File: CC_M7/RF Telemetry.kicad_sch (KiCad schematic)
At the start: 33 parts, among them J9 SMA_CONNECTOR, U6 nRF52820-QDxx, U7 NRF21540-QDAA-R7, Y2 32MHz

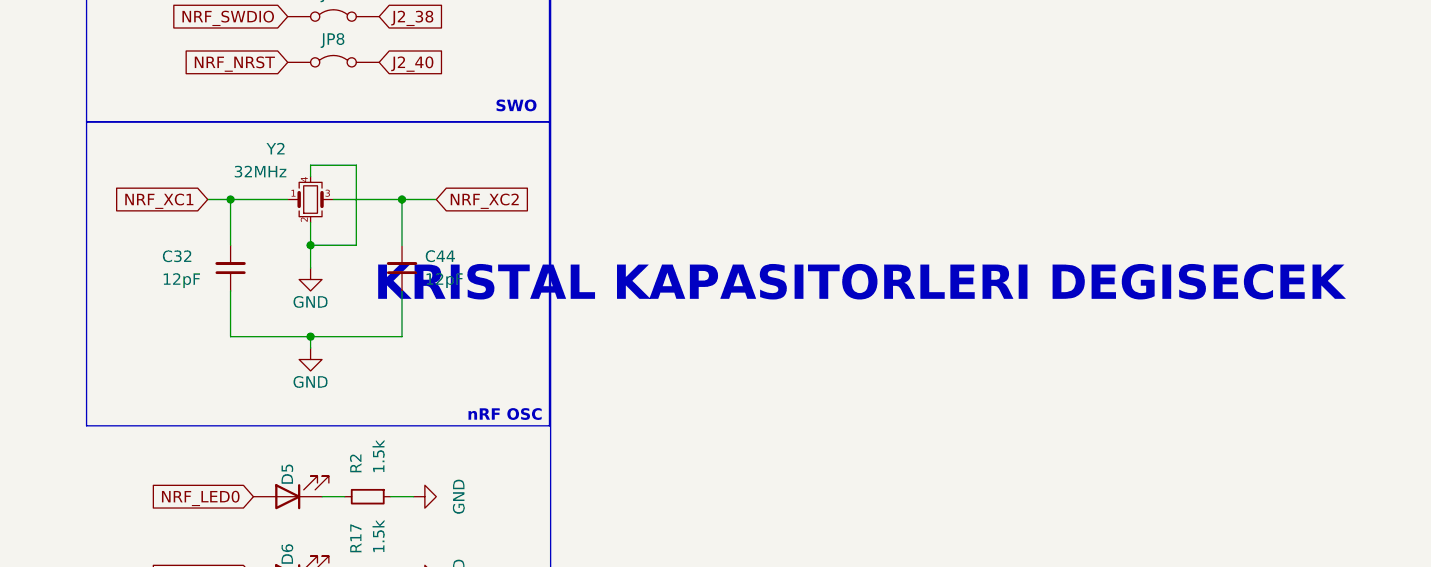
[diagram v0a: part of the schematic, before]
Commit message: USB Pullup added, oscillator capacitors updated.
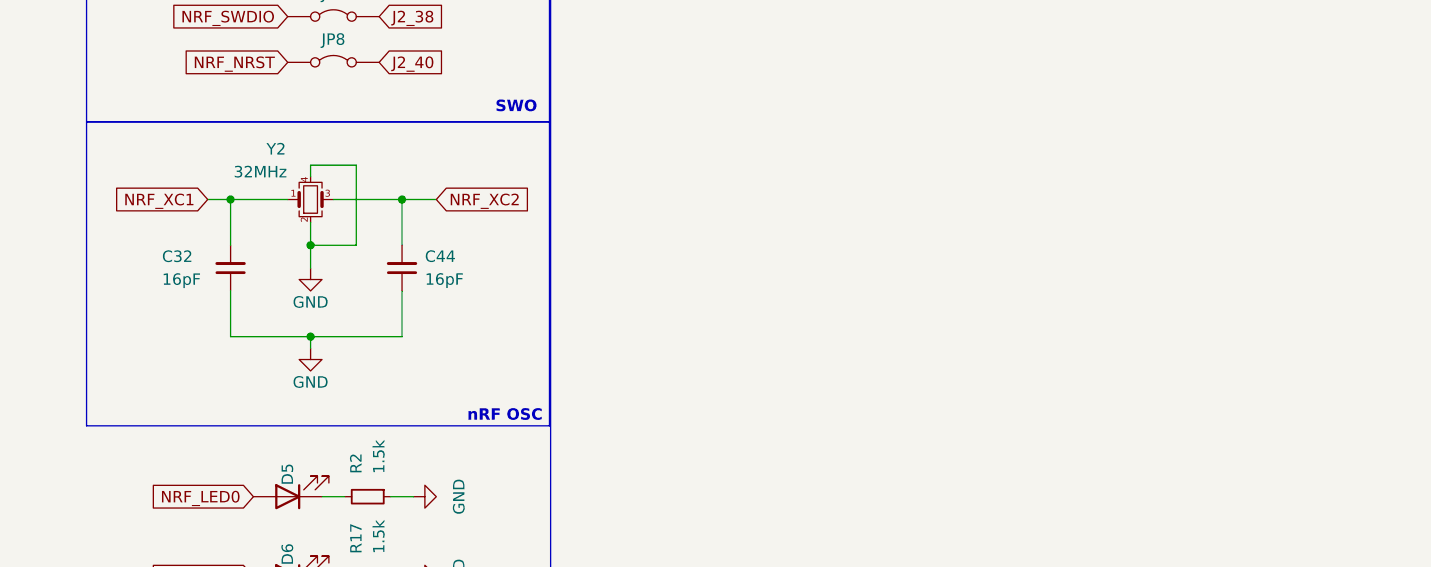
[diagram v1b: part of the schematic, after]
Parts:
- C32, C44: value 12pF -> 16pF
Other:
- note removed: "KRISTAL KAPASITORLERI DEGISECEK"
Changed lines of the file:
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@@
 		)
 	)
-	(text "KRISTAL KAPASITORLERI DEGISECEK\n"
-		(exclude_from_sim no)
-		(at 232.41 99.695 0)
-		(effects
-			(font
-				(size 3.81 3.81)
-				(thickness 0.762)
-				(bold yes)
-			)
-		)
-	)
 	(text "SWO"
 		(exclude_from_sim no)
@@
 			)
 		)
-		(property "Value" "12pF"
+		(property "Value" "16pF"
 			(at 184.15 99.0535 0)
 			(effects
@@
 			)
 		)
-		(property "Value" "12pF"
+		(property "Value" "16pF"
 			(at 154.94 99.06 0)
 			(effects

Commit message: warning check
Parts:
- JP5, JP6, JP7, JP8: footprint Jumper:SolderJumper-2_P1.3mm_Open_TrianglePad1.0x1.5mm -> jmpertest:jmpertest
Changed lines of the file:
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@@
 			)
 		)
-		(property "Footprint" "Jumper:SolderJumper-2_P1.3mm_Open_TrianglePad1.0x1.5mm"
+		(property "Footprint" "jmpertest:jmpertest"
 			(at 173.99 64.77 0)
 			(effects
@@
 			)
 		)
-		(property "Footprint" "Jumper:SolderJumper-2_P1.3mm_Open_TrianglePad1.0x1.5mm"
+		(property "Footprint" "jmpertest:jmpertest"
 			(at 173.99 69.85 0)
 			(effects
@@
 			)
 		)
-		(property "Footprint" "Jumper:SolderJumper-2_P1.3mm_Open_TrianglePad1.0x1.5mm"
+		(property "Footprint" "jmpertest:jmpertest"
 			(at 173.99 59.69 0)
 			(effects
@@
 			)
 		)
-		(property "Footprint" "Jumper:SolderJumper-2_P1.3mm_Open_TrianglePad1.0x1.5mm"
+		(property "Footprint" "jmpertest:jmpertest"
 			(at 173.99 74.93 0)
 			(effects
